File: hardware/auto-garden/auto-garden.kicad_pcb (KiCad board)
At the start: 2 copper layers, 71.1 x 55.9 mm, 32 parts, among them J1 Conn_01x02_Female, J2 Conn_01x06_Female, J3 Conn_01x03_Female, J4 Conn_01x03_Male, J5 Screw_Terminal_01x02, J6 Screw_Terminal_01x02, Q1 Q_PMOS_DGS, Q2 Q_NMOS_DGS, Q3 Q_PMOS_DGS, Q4 Q_NMOS_DGS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

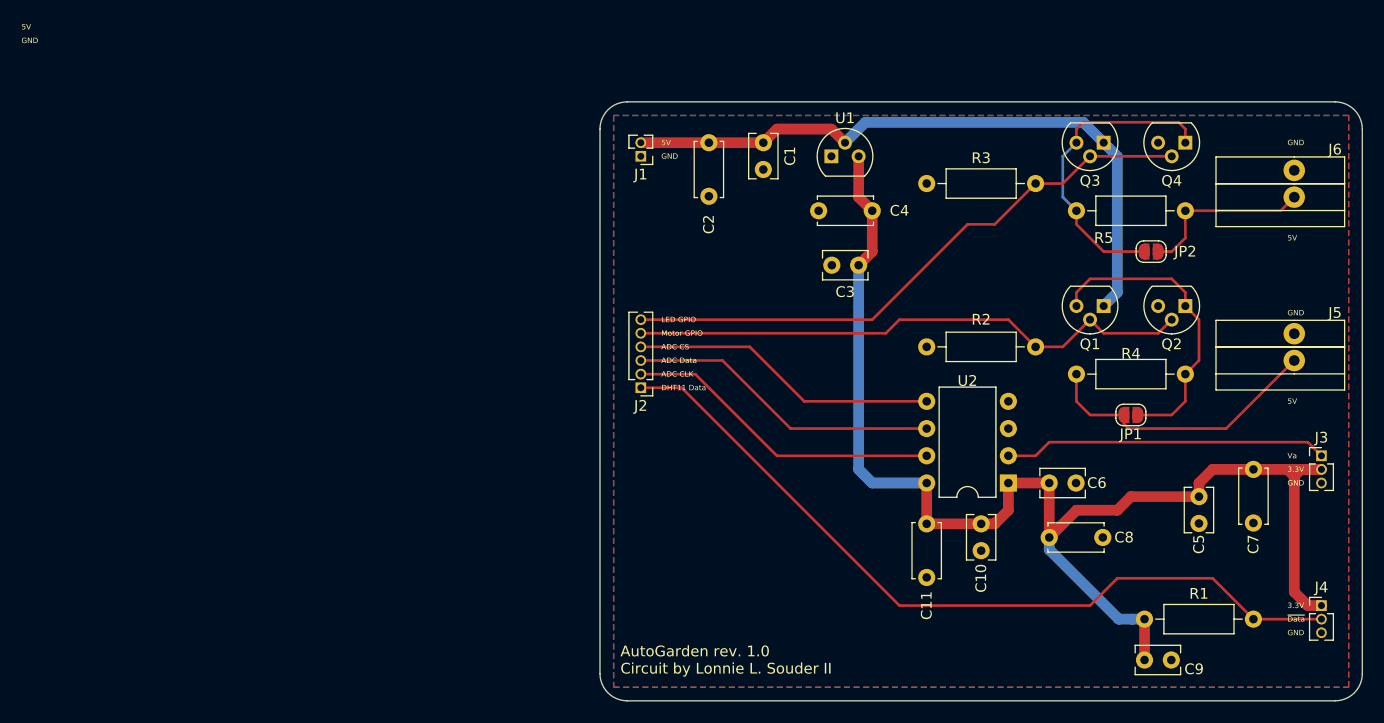
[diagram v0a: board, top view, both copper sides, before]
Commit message: rerouted with new pin headers
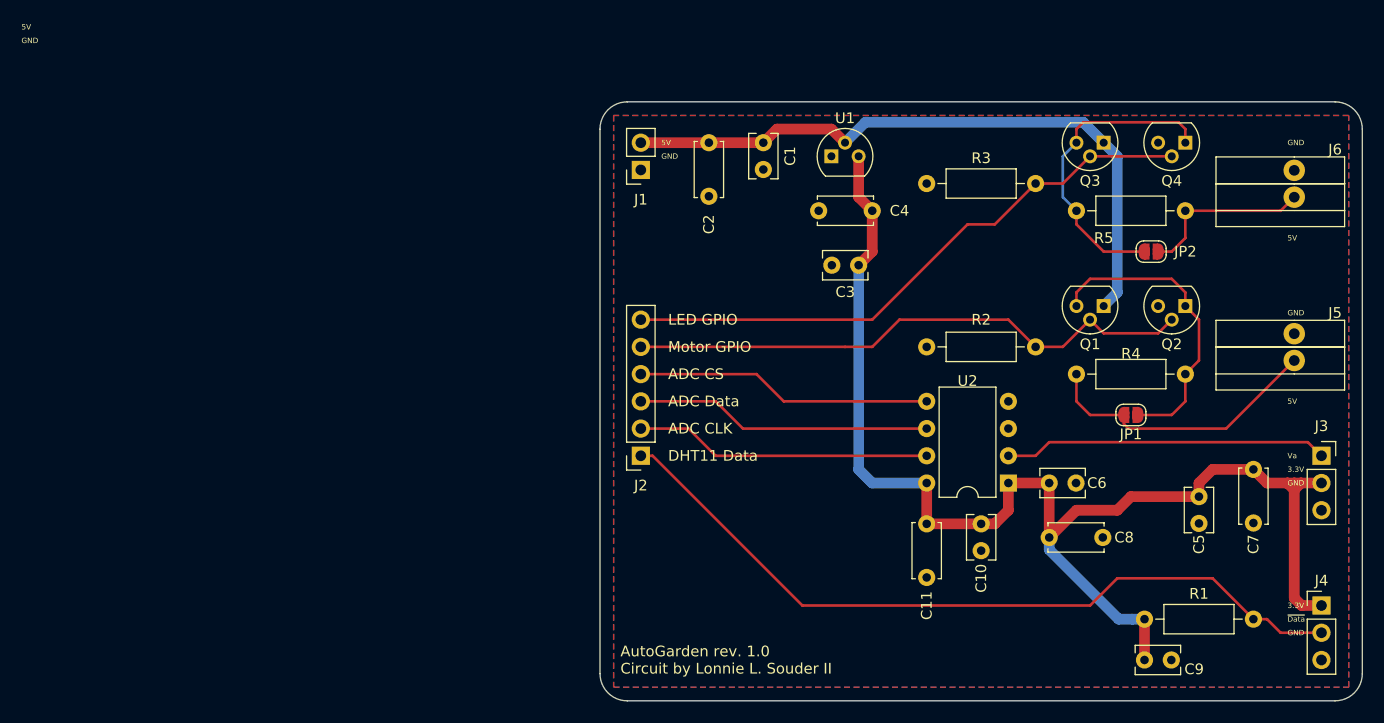
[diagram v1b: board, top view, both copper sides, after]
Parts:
- removed REF**: OSHW-Logo2_7.3x6mm_SilkScreen, Symbol:OSHW-Logo2_7.3x6mm_SilkScreen
- removed REF**: KiCad-Logo2_5mm_SilkScreen, Symbol:KiCad-Logo2_5mm_SilkScreen
- J1: footprint Connector_PinHeader_1.27mm:PinHeader_1x02_P1.27mm_Vertical -> Connector_PinSocket_2.54mm:PinSocket_1x02_P2.54mm_Vertical
- J2: footprint Connector_PinHeader_1.27mm:PinHeader_1x06_P1.27mm_Vertical -> Connector_PinSocket_2.54mm:PinSocket_1x06_P2.54mm_Vertical
- J3: footprint Connector_PinHeader_1.27mm:PinHeader_1x03_P1.27mm_Vertical -> Connector_PinSocket_2.54mm:PinSocket_1x03_P2.54mm_Vertical
- J4: footprint Connector_PinHeader_1.27mm:PinHeader_1x03_P1.27mm_Vertical -> Connector_PinHeader_2.54mm:PinHeader_1x03_P2.54mm_Vertical
- moved J2 6.35 mm to (121.3, 106.0)
- moved J1 1.27 mm to (121.3, 79.4)
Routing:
- net +3V3: track 126.0 -> 121.7 mm
- net P2_CLK: track 29.8 -> 27.7 mm
- net ~P1: track 74.5 -> 72.4 mm
- net P3_data: track 29.3 -> 27.7 mm
- net P4_~CS: track 28.8 -> 27.7 mm
- net ~P5: track 53.2 -> 53.7 mm
